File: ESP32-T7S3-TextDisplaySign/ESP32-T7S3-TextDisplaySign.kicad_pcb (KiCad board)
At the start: 2 copper layers, 105.4 x 76.2 mm, 34 parts, among them J101 Displays, J102 Micro_SD_Card_Det, J501 Vcc CS2 CS1 C D RS RST A K G, J801 RJ45, J802 RJ45, Q101 PZT2222A, T801 - 15 in +, T802 - 15 out +, U201 TTGO-T7_S3-V1.1, U301 AP63205, U801 TCAN332DR

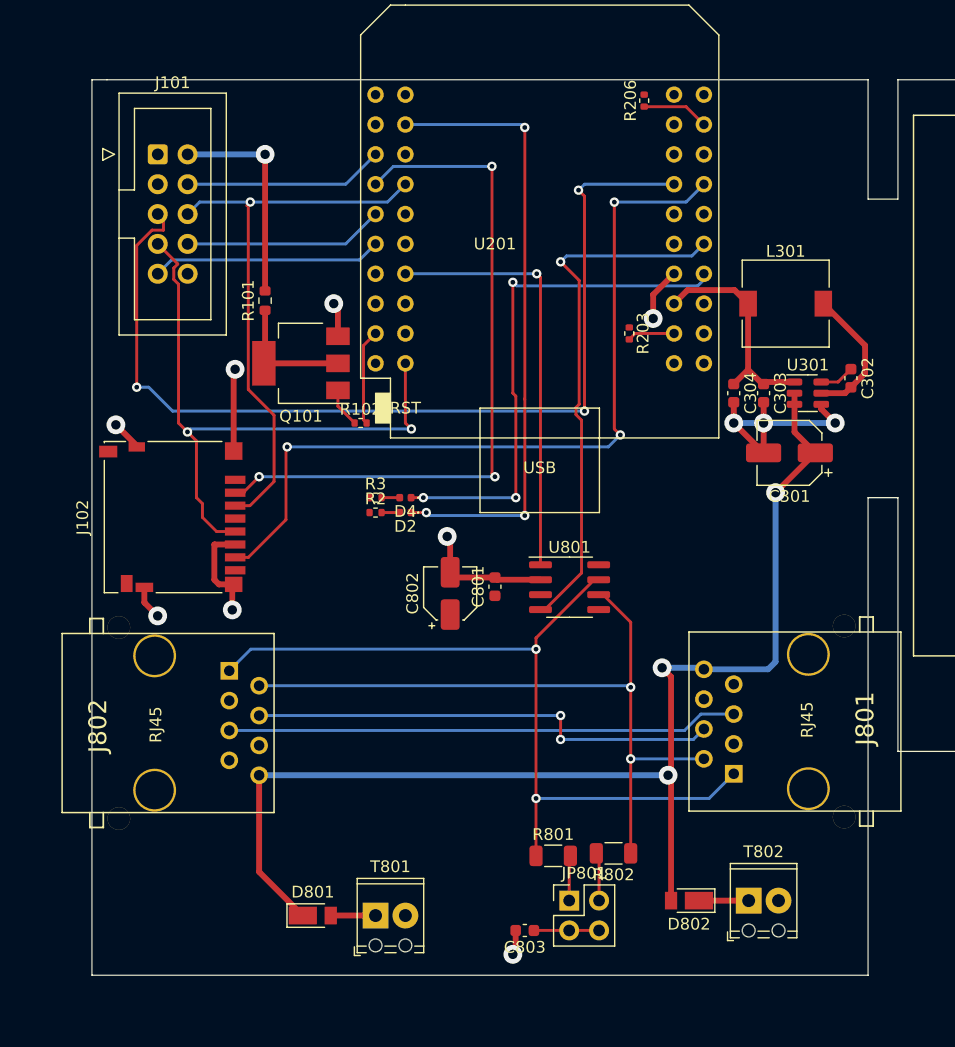
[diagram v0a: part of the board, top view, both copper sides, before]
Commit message: Completed board layout.
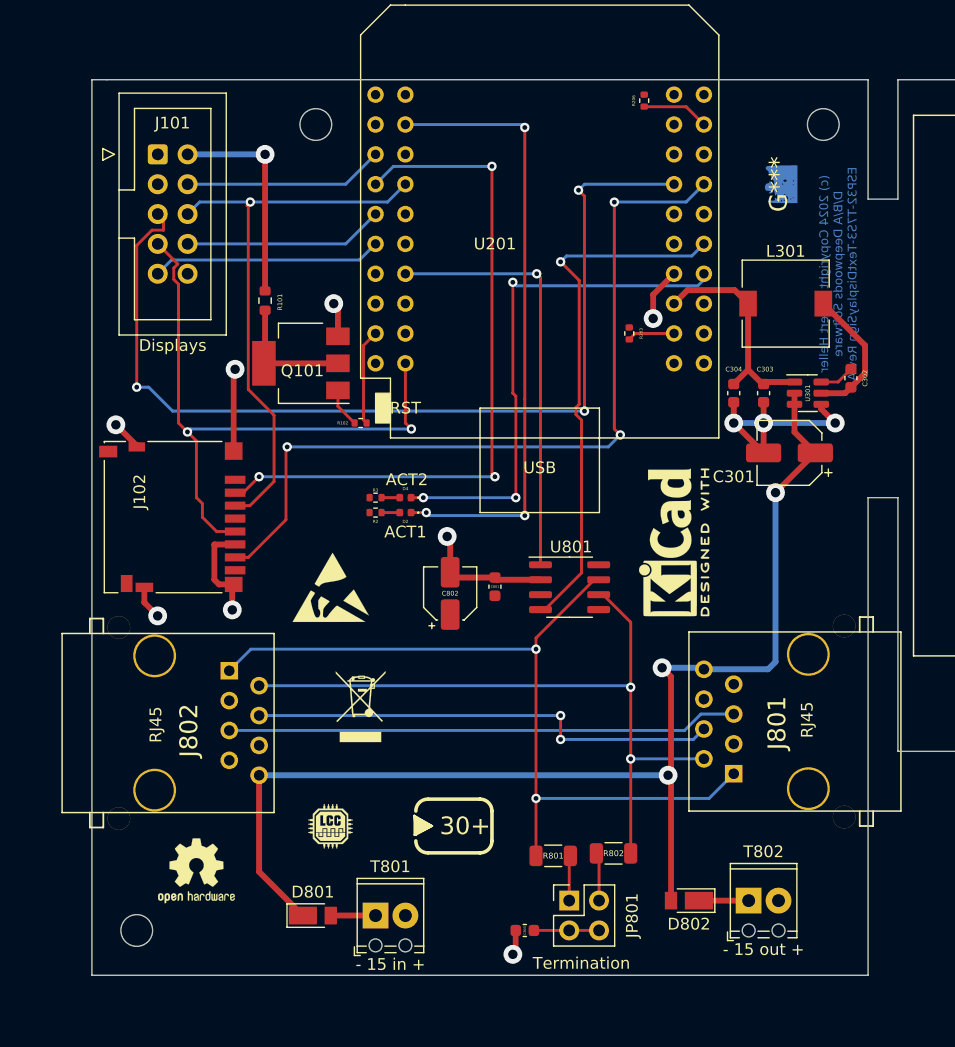
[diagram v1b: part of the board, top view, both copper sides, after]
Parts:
- added G***: LCC, LCC:LCC_LOGO_4.5x4.5, F.Cu at (128.3, 90.2)
- added G***: LOGO, DWS:DWSLogoBCU, F.Cu at (166.4, 35.6)
- added REF**: PowerLabel-30Plus, Power:PowerLabel-30Plus, F.Cu at (139.7, 90.2)
- added REF**: MountingHole_2.7mm_M2.5, MountingHole:MountingHole_2.7mm_M2.5, F.Cu at (170.2, 30.5)
- added REF**: ESD-Logo_6.6x6mm_SilkScreen, Symbol:ESD-Logo_6.6x6mm_SilkScreen, F.Cu at (128.3, 69.8)
- added REF**: MountingHole_2.7mm_M2.5, MountingHole:MountingHole_2.7mm_M2.5, F.Cu at (127.0, 30.5)
- added REF**: MountingHole_2.7mm_M2.5, MountingHole:MountingHole_2.7mm_M2.5, F.Cu at (111.8, 99.1)
- added REF**: WEEE-Logo_4.2x6mm_SilkScreen, Symbol:WEEE-Logo_4.2x6mm_SilkScreen, F.Cu at (130.8, 80.0)
- added REF**: KiCad-Logo2_5mm_SilkScreen, Symbol:KiCad-Logo2_5mm_SilkScreen, F.Cu at (157.5, 66.0)
- added REF**: OSHW-Logo2_7.3x6mm_SilkScreen, Symbol:OSHW-Logo2_7.3x6mm_SilkScreen, F.Cu at (116.8, 94.0)
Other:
- board text added: "(c) 2024 Copyright Robert Heller D/B/A Deepwoods Software ESP32-T7S3-TextDisplaySign Rev A"

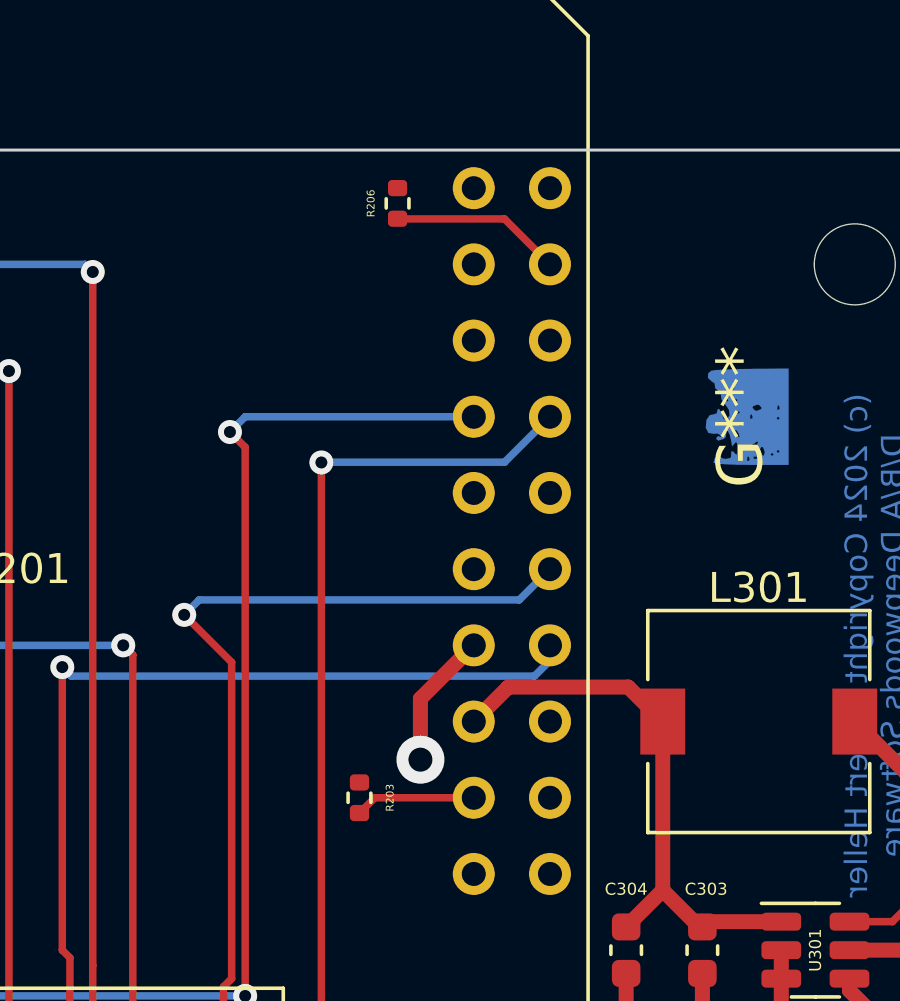
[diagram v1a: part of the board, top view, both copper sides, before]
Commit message: Remove unused I2C connections.
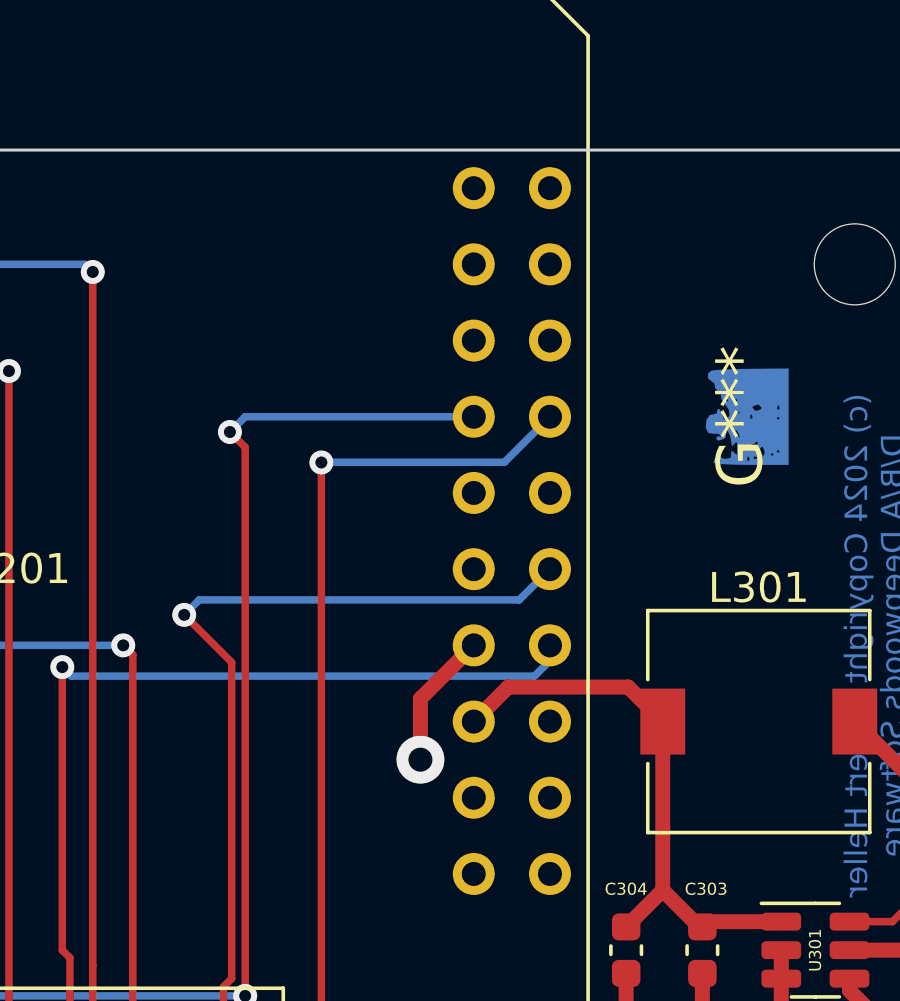
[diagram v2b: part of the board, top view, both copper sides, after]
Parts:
- removed R203, R206: 2.4K, Resistor_SMD:R_0402_1005Metric
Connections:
- U201 pad 24: /Processor/GPIO3/SCL -> unconnected-(U201-Pad24)
- U201 pad 37: /Processor/GPIO40/SDA -> unconnected-(U201-Pad37)
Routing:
- net /Processor/GPIO3/SCL: track 5.71 -> 0.00 mm
- net /Processor/GPIO40/SDA: track 4.02 -> 0.00 mm
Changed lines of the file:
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@@
   (net 46 "Net-(Q101-Pad2)")
   (net 47 "/Backlight")
-  (net 48 "/Processor/GPIO40{slash}SDA")
-  (net 49 "/Processor/GPIO3{slash}SCL")
+  (net 48 "unconnected-(U201-Pad24)")
+  (net 49 "unconnected-(U201-Pad37)")
   (net 50 "unconnected-(U201-Pad40)")
   (net 51 "unconnected-(U201-Pad39)")
@@
       (net 60 "unconnected-(U201-Pad23)") (pinfunction "RXD") (pintype "passive+no_connect"))
     (pad "24" thru_hole circle locked (at 13.97 -8.89 270) (size 1.4 1.4) (drill 0.8) (layers *.Cu *.Mask)
-      (net 49 "/Processor/GPIO3{slash}SCL") (pinfunction "IO_3") (pintype "bidirectional"))
+      (net 48 "unconnected-(U201-Pad24)") (pinfunction "IO_3") (pintype "bidirectional"))
     (pad "25" thru_hole circle locked (at 11.43 -6.35 270) (size 1.4 1.4) (drill 0.8) (layers *.Cu *.Mask)
       (net 59 "unconnected-(U201-Pad25)") (pinfunction "IO_14") (pintype "bidirectional+no_connect"))
@@
       (net 53 "unconnected-(U201-Pad36)") (pinfunction "IO_2") (pintype "bidirectional+no_connect"))
     (pad "37" thru_hole circle locked (at 11.43 8.89 270) (size 1.4 1.4) (drill 0.8) (layers *.Cu *.Mask)
-      (net 48 "/Processor/GPIO40{slash}SDA") (pinfunction "TD0") (pintype "passive"))
+      (net 49 "unconnected-(U201-Pad37)") (pinfunction "TD0") (pintype "passive"))
     (pad "38" thru_hole circle locked (at 13.97 8.89 270) (size 1.4 1.4) (drill 0.8) (layers *.Cu *.Mask)
       (net 52 "unconnected-(U201-Pad38)") (pinfunction "IO_1") (pintype "passive+no_connect"))
@@
     )
   )
-  (footprint "Resistor_SMD:R_0402_1005Metric" (layer "F.Cu")
-    (at 154.94 28.448 90)
-    (descr "Resistor SMD 0402 (1005 Metric), square (rectangular) end terminal, IPC_7351 nominal, (Body size source: IPC-SM-782 page 72, https://www.pcb-3d.com/wordpress/wp-content/uploads/ipc-sm-782a_amendment_1_and_2.pdf), generated with kicad-footprint-generator")
-    (tags "resistor")
-    (property "Mouser Part Number" "603-RC0402FR-072K4L")
-    (property "Sheetfile" "Processor.kicad_sch")
-    (property "Sheetname" "Processor")
-    (attr smd)
-    (fp_text reference "R206" (at 0 -0.889 90) (layer "F.SilkS")
-      (effects (font (size 0.26 0.26) (thickness 0.04)))
-    )
-    (fp_text value "2.4K" (at 0 1.016 90) (layer "F.Fab")
-      (effects (font (size 0.5 0.5) (thickness 0.075)))
-    )
-    (fp_text user "${REFERENCE}" (at 0 -0.889 90) (layer "F.Fab")
-      (effects (font (size 0.26 0.26) (thickness 0.04)))
-    )
-    (fp_line (start -0.153641 0.38) (end 0.153641 0.38) (layer "F.SilkS") (width 0.12))
-    (fp_line (start -0.153641 -0.38) (end 0.153641 -0.38) (layer "F.SilkS") (width 0.12))
-    (fp_line (start 0.93 0.47) (end -0.93 0.47) (layer "F.CrtYd") (width 0.05))
-    (fp_line (start 0.93 -0.47) (end 0.93 0.47) (layer "F.CrtYd") (width 0.05))
-    (fp_line (start -0.93 0.47) (end -0.93 -0.47) (layer "F.CrtYd") (width 0.05))
-    (fp_line (start -0.93 -0.47) (end 0.93 -0.47) (layer "F.CrtYd") (width 0.05))
-    (fp_line (start 0.525 0.27) (end -0.525 0.27) (layer "F.Fab") (width 0.1))
-    (fp_line (start 0.525 -0.27) (end 0.525 0.27) (layer "F.Fab") (width 0.1))
-    (fp_line (start -0.525 -0.27) (end 0.525 -0.27) (layer "F.Fab") (width 0.1))
-    (fp_line (start -0.525 0.27) (end -0.525 -0.27) (layer "F.Fab") (width 0.1))
-    (pad "1" smd roundrect (at -0.51 0 90) (size 0.54 0.64) (layers "F.Cu" "F.Paste" "F.Mask") (roundrect_rratio 0.25)
-      (net 49 "/Processor/GPIO3{slash}SCL") (pintype "passive"))
-    (pad "2" smd roundrect (at 0.51 0 90) (size 0.54 0.64) (layers "F.Cu" "F.Paste" "F.Mask") (roundrect_rratio 0.25)
-      (net 6 "+3V3") (pintype "passive"))
-    (model "${KICAD6_3DMODEL_DIR}/Resistor_SMD.3dshapes/R_0402_1005Metric.wrl"
-      (offset (xyz 0 0 0))
-      (scale (xyz 1 1 1))
-      (rotate (xyz 0 0 0))
-    )
-  )
   (footprint "Diode_SMD:D_PowerDI-123" (layer "F.Cu")
     (at 158.75 96.52 180)
@@
   )
   (footprint "Resistor_SMD:R_0402_1005Metric" (layer "F.Cu")
-    (at 153.67 48.26 -90)
-    (descr "Resistor SMD 0402 (1005 Metric), square (rectangular) end terminal, IPC_7351 nominal, (Body size source: IPC-SM-782 page 72, https://www.pcb-3d.com/wordpress/wp-content/uploads/ipc-sm-782a_amendment_1_and_2.pdf), generated with kicad-footprint-generator")
-    (tags "resistor")
-    (property "Mouser Part Number" "603-RC0402FR-072K4L")
-    (property "Sheetfile" "Processor.kicad_sch")
-    (property "Sheetname" "Processor")
-    (attr smd)
-    (fp_text reference "R203" (at 0 -1.016 90) (layer "F.SilkS")
-      (effects (font (size 0.26 0.26) (thickness 0.04)))
-    )
-    (fp_text value "2.4K" (at 0 0.889 90) (layer "F.Fab")
-      (effects (font (size 0.5 0.5) (thickness 0.075)))
-    )
-    (fp_text user "${REFERENCE}" (at 0 -1.016 90) (layer "F.Fab")
-      (effects (font (size 0.26 0.26) (thickness 0.04)))
-    )
-    (fp_line (start -0.153641 0.38) (end 0.153641 0.38) (layer "F.SilkS") (width 0.12))
-    (fp_line (start -0.153641 -0.38) (end 0.153641 -0.38) (layer "F.SilkS") (width 0.12))
-    (fp_line (start -0.93 0.47) (end -0.93 -0.47) (layer "F.CrtYd") (width 0.05))
-    (fp_line (start 0.93 0.47) (end -0.93 0.47) (layer "F.CrtYd") (width 0.05))
-    (fp_line (start 0.93 -0.47) (end 0.93 0.47) (layer "F.CrtYd") (width 0.05))
-    (fp_line (start -0.93 -0.47) (end 0.93 -0.47) (layer "F.CrtYd") (width 0.05))
-    (fp_line (start 0.525 0.27) (end -0.525 0.27) (layer "F.Fab") (width 0.1))
-    (fp_line (start -0.525 0.27) (end -0.525 -0.27) (layer "F.Fab") (width 0.1))
-    (fp_line (start -0.525 -0.27) (end 0.525 -0.27) (layer "F.Fab") (width 0.1))
-    (fp_line (start 0.525 -0.27) (end 0.525 0.27) (layer "F.Fab") (width 0.1))
-    (pad "1" smd roundrect (at -0.51 0 270) (size 0.54 0.64) (layers "F.Cu" "F.Paste" "F.Mask") (roundrect_rratio 0.25)
-      (net 6 "+3V3") (pintype "passive"))
-    (pad "2" smd roundrect (at 0.51 0 270) (size 0.54 0.64) (layers "F.Cu" "F.Paste" "F.Mask") (roundrect_rratio 0.25)
-      (net 48 "/Processor/GPIO40{slash}SDA") (pintype "passive"))
-    (model "${KICAD6_3DMODEL_DIR}/Resistor_SMD.3dshapes/R_0402_1005Metric.wrl"
-      (offset (xyz 0 0 0))
-      (scale (xyz 1 1 1))
-      (rotate (xyz 0 0 0))
-    )
-  )
-  (footprint "Resistor_SMD:R_0402_1005Metric" (layer "F.Cu")
     (at 132.08 63.5)
     (descr "Resistor SMD 0402 (1005 Metric), square (rectangular) end terminal, IPC_7351 nominal, (Body size source: IPC-SM-782 page 72, https://www.pcb-3d.com/wordpress/wp-content/uploads/ipc-sm-782a_amendment_1_and_2.pdf), generated with kicad-footprint-generator")
@@
   (segment (start 131.055 49.285) (end 131.055 55.615) (width 0.25) (layer "F.Cu") (net 47))
   (segment (start 132.08 48.26) (end 131.055 49.285) (width 0.25) (layer "F.Cu") (net 47))
-  (segment (start 157.48 48.26) (end 154.18 48.26) (width 0.25) (layer "F.Cu") (net 48))
-  (segment (start 154.18 48.26) (end 153.67 48.77) (width 0.25) (layer "F.Cu") (net 48))
-  (segment (start 158.505 28.965) (end 154.947 28.965) (width 0.25) (layer "F.Cu") (net 49))
-  (segment (start 154.947 28.965) (end 154.94 28.958) (width 0.25) (layer "F.Cu") (net 49))
-  (segment (start 160.02 30.48) (end 158.505 28.965) (width 0.25) (layer "F.Cu") (net 49))
   (segment (start 149.606 68.640751) (end 146.491751 71.755) (width 0.25) (layer "F.Cu") (net 54))
   (segment (start 147.828 42.164) (end 149.41 43.746) (width 0.25) (layer "F.Cu") (net 54))
